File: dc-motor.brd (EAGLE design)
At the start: 160 x 100 mm, 0 parts

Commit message: Erste Version des Schaltplans (Noch nicht fertig)
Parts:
- added C1, C10, C13, C14, C3, C9: 100nF, Capacitor:0805
- added C11: 1µF, Capacitor:0805
- added C12: 0,22µF, Capacitor:0805
- added C2, C7, C8: 10nF, Capacitor:0805
- added C4: 100µF/50V, Capacitor:E5-13
- added C5: 47µF, Capacitor:E5-13
- added C6: 100µF, Capacitor:E5-13
- added D1: 1N4007, Diode:RM10DR1
- added D2: 1,5KB33CA, Diode:CB417-15
- added F1: F2A, fuse:F457
- added F2: T0,5A, fuse:F457
- added G1: 8MHz, Crystals:HC33U-V
- added H1, H2: MOUNT-PAD-ROUND3.0, Holes:3,0-PAD
- added IC1: MEGA8-P, atmel:DIL28-3
- added JP1, JP2, JP3: (no value), jumper:JP2Q
- added R1: (no value), DC-DC-converter:SIP3
- added R10, R3, R8, R9: 2k7, Resistor:0805
- added R11, R4, R6: 39k, Resistor:0805
- added R12, R5, R7: 10k, Resistor:0805
- added R13, R14, R15: 3,3k, Resistor:0805
- added R16, R17, R18, R19: 180R, Resistor:0805
- added R2: 0,05R, Resistor:SMS-0
- added R20, R21, R22, R23: 250R, Resistor:0805
- added S1: (no value), Switch:B3F-10XX
- added S2, S3: (no value), Switch:1_POL_ABGW
- added U$17: MAX4080, Sensorics:MAX4080
- added U$28: ACPL-247, Optoelectronic:SOIC16
- added U$3: DRV-8800, DRV-8800:TSSOP16
- added X1: (no value), con-subd:F09HP
- added X2: (no value), con-subd:M09HP
- added X3, X4: RIA_3POL, Connector:RIA_3POL
- added X5: RIA_2POL, Connector:RIA_2POL
- added X6: JUMP1-4, Connector:JUMP1-4
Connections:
- new net +24V: C5.+, D1.K, D2.C, F1.1, F2.2, R1.1, R11.2
- new net GND: C1.1, C10.1, C12.1, C14.1, C2.1, C4.-, C5.-, C6.-, C7.1, C8.1, C9.1, D1.A, D2.A, IC1.22, IC1.8, R1.2, R10.1, R12.1, R15.2, R3.1, R5.1, R7.1, R8.1, R9.1, S1.3, S1.4, U$17.4, U$28.2, U$28.4, U$28.6, U$28.8, U$3.12, U$3.2, X1.G1, X1.G2, X2.6, X2.7, X2.G2, X5.P$2, X6.4
- new net N$1: F1.2, X2.1, X5.P$1
- new net N$10: C13.1, C14.2, C4.+, R2.2, U$17.8, U$3.8
- new net N$11: IC1.18, R6.1, R7.2
- new net N$12: R6.2, X2.9
- new net N$13: R4.2, X2.8
- new net N$14: IC1.23, U$17.5
- new net N$15: IC1.17, R8.2, S3.S1
- new net N$16: C3.1
- new net N$17: IC1.16, R3.2, S2.S1
- new net N$18: IC1.15, JP1.1, JP1.3, R9.2
- new net N$19: JP1.2, JP2.2, X1.3
- new net N$2: G1.2, IC1.9
- new net N$20: JP1.4, JP2.4, X1.2
- new net N$21: H1.B3,0
- new net N$22: IC1.1, S1.1, S1.2
- new net N$23: C8.2, IC1.20
- new net N$24: C10.2, H2.B3,0
- new net N$25: IC1.14, JP2.1, JP2.3, R10.2
- new net N$26: C11.2, U$3.10
- new net N$27: C11.1, U$3.11
- new net N$28: C12.2, U$3.14
- new net N$29: C13.2, U$3.13
- new net N$3: G1.1, IC1.10
- new net N$30: IC1.25
- new net N$31: R23.1, U$3.4
- new net N$32: R21.1, U$3.1
- new net N$33: R14.1, U$3.15
- new net N$34: R13.1, R20.1, U$3.3
- new net N$35: U$28.15
- new net N$36: R15.1, U$3.7
- new net N$38: IC1.11, R16.1
- new net N$39: IC1.6, R19.1
- new net N$4: IC1.2, X6.1
- new net N$40: IC1.5, R18.2
- new net N$41: R17.2
- new net N$42: R16.2, U$28.1
- new net N$43: R17.1, U$28.3
- new net N$44: R18.1, U$28.5
- new net N$45: R19.2, U$28.7
- new net N$46: R23.2, U$28.13
- new net N$47: R21.2, U$28.11
- new net N$48: R22.1, U$3.16
- new net N$49: R20.2, U$28.9
- new net N$5: JP3.1, JP3.4, U$3.6, X1.4
- new net N$50: IC1.24, R11.1, R12.2
- new net N$51: IC1.26
- new net N$52: IC1.27
- new net N$53: IC1.28
- new net N$6: F2.1, R2.1, U$17.1
- new net N$7: JP3.2, JP3.3, U$3.9, X1.5
- new net N$8: IC1.3, X6.2
- new net N$9: IC1.19, R4.1, R5.2
- new net VDD: C1.2, C2.2, C3.2, C6.+, C7.2, IC1.21, IC1.7, R1.3, R13.2, R14.2, S2.S2, S3.S2, U$17.2, U$28.10, U$28.12, U$28.14, U$28.16, X1.1, X6.3

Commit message: Schaltplan Fertig
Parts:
- added C15, C16: 15pF, Capacitor:0805
- added H3: MOUNT-HOLE3.2, Holes:3,2
- added R24, R28, R31, R32: 2k2, Resistor:0805
- added R25, R26, R29, R30: 10R, Resistor:0805
- added R27: 180R, Resistor:0805
- added R33, R34, R35: 2k7, Resistor:0805
- added U$34: ACPL-247, Optoelectronic:SOIC16
- added U$35, U$38: IRF7341, Transistor:SO08-IRF
- added X7, X8: PFVERB10, Connector:PFVERB10
- C11: value 1µF -> 100nF
- IC1: value MEGA8-P -> MEGA32-A; device atmel:DIL28-3 -> atmel:TQFP44
- R13: value 3,3k -> 2k7
- moved JP3 224.9 mm to (130.8, 21.6)
- moved C13 220.3 mm to (111.8, 16.5)
- moved R2 215.6 mm to (114.3, 35.6)
- moved R13 214.5 mm to (104.1, 21.6)
- moved JP2 214.5 mm to (130.8, 43.2)
- moved X2 213.2 mm to (149.9, 49.5), turned to 90 degrees
- moved C12 201.7 mm to (116.8, 16.5), turned to 180 degrees
- moved R6 200.7 mm to (134.6, 54.6)
- moved R7 200.7 mm to (129.5, 54.6)
- moved X4 199.3 mm to (157.5, 94.0), turned to 90 degrees
- moved U$3 194.8 mm to (113.0, 22.9), turned to 180 degrees
- moved R4 191.6 mm to (134.6, 50.8)
- moved R5 191.6 mm to (129.5, 50.8)
- moved R21 189.4 mm to (123.2, 25.4), turned to 90 degrees
- moved X5 189.1 mm to (129.5, 8.89), turned to 270 degrees
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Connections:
- removed net N$14 (its old number): IC1.23, U$17.5
- removed net N$22: IC1.1, S1.1, S1.2
- removed net N$30: IC1.25
- removed net N$32 (its old number): R21.1, U$3.1
- removed net N$39: IC1.6, R19.1
- removed net N$40: IC1.5, R18.2
- removed net N$41: R17.2
- removed net N$51: IC1.26
- removed net N$52: IC1.27
- removed net N$53: IC1.28
- new net ENDLAGE_A: IC1.41, R32.1, U$35.2
- new net ENDLAGE_B: IC1.40, R31.1, U$35.4
- new net FAEHRTNACHA: IC1.36, X7.5
- new net FAEHRTNACHB: IC1.35, X7.6
- new net LOCAL/REMOTE: IC1.33, X7.8
- new net MISO: IC1.2, R18.2, X8.3
- new net MOSI: IC1.1, R19.1, X8.9
- new net MOTORSICHERUNGLED: IC1.37, X7.4
- new net MOTORSTOP: IC1.34, X7.7
- new net N$10: IC1.31, U$17.5
- new net N$37: U$34.14, X2.5
- new net N$54: R26.2, X2.4
- new net N$55: R25.2, X2.3
- new net N$57: U$34.3
- new net N$58: U$34.13, U$38.1, U$38.3
- new net N$59: R25.1, U$38.5, U$38.6
- new net N$60: C8.2, IC1.27
- new net N$61: R27.2, U$34.4
- new net N$62: R26.1, U$38.7, U$38.8
- new net N$67: R29.1, X3.P$1
- new net N$68: R30.1, X4.P$1
- new net N$69: R30.2, U$35.5, U$35.6
- new net N$70: U$35.3, X4.P$2
- new net N$71: R29.2, U$35.7, U$35.8
- new net N$72: U$35.1, X3.P$2
- new net N$77: R21.1, R35.2, U$3.1
- new net RESET: IC1.4, S1.1, S1.2, X8.6
- new net SCK: IC1.3, R17.2, X8.1
- net +24V: now also X7.3
- net GND: now also C15.2, C16.2, C3.1, IC1.18, IC1.28, IC1.39, IC1.6, R13.1, R24.2, R27.1, R28.2, R31.2, R32.2, R33.1, R34.1, R35.1, X3.P$3, X4.P$3, X7.10, X8.10, X8.2; no longer IC1.22, IC1.8
- net N$11: now also IC1.22; no longer IC1.18
- net N$15: now also IC1.23; no longer IC1.17
- net N$16: now also IC1.42, R24.1, U$38.2; no longer C3.1
- net N$17: now also IC1.24; no longer IC1.16
- net N$18: now also IC1.25; no longer IC1.15
- net N$19: now also X7.1
- net N$2: now also C15.1, G1.1, IC1.8; no longer G1.2, IC1.9
- net N$20: now also X7.2
- net N$21: now also C9.2
- net N$23: now also IC1.43, R28.1, U$38.4; no longer C8.2, IC1.20
- net N$25: now also IC1.26; no longer IC1.14
- net N$3: now also C16.1, G1.2, IC1.7; no longer G1.1, IC1.10
- net N$31: now also R34.2
- net N$34: now also R13.2; no longer R13.1
- net N$35: now also R22.2
- net N$38: now also IC1.44; no longer IC1.11
- net N$4: now also IC1.9; no longer IC1.2
- net N$48: now also R33.2
- net N$50: now also IC1.32; no longer IC1.24
- net N$6: now also IC1.30
- net N$8: now also IC1.10; no longer IC1.3
- net N$9: now also IC1.21; no longer IC1.19
- net VDD: now also IC1.17, IC1.29, IC1.38, IC1.5, X7.9, X8.4; no longer IC1.21, IC1.7, R13.2
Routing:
- net N$1: track 0.00 -> 192.5 mm, vias 0 -> 1
- net +24V: track 0.00 -> 84.8 mm
- net VDD: track 0.00 -> 41.4 mm
- net N$46: track 0.00 -> 9.42 mm
- net N$24: track 0.00 -> 9.21 mm
- net N$21: track 0.00 -> 9.21 mm
- net N$45: track 0.00 -> 8.14 mm
- net N$44: track 0.00 -> 7.51 mm
- net N$35: track 0.00 -> 7.18 mm
- net N$43: track 0.00 -> 5.74 mm
- net N$42: track 0.00 -> 5.29 mm
- net GND: track 0.00 -> 0.72 mm
- added copper zone on layer 1, net GND
- added copper zone on layer 16, net GND

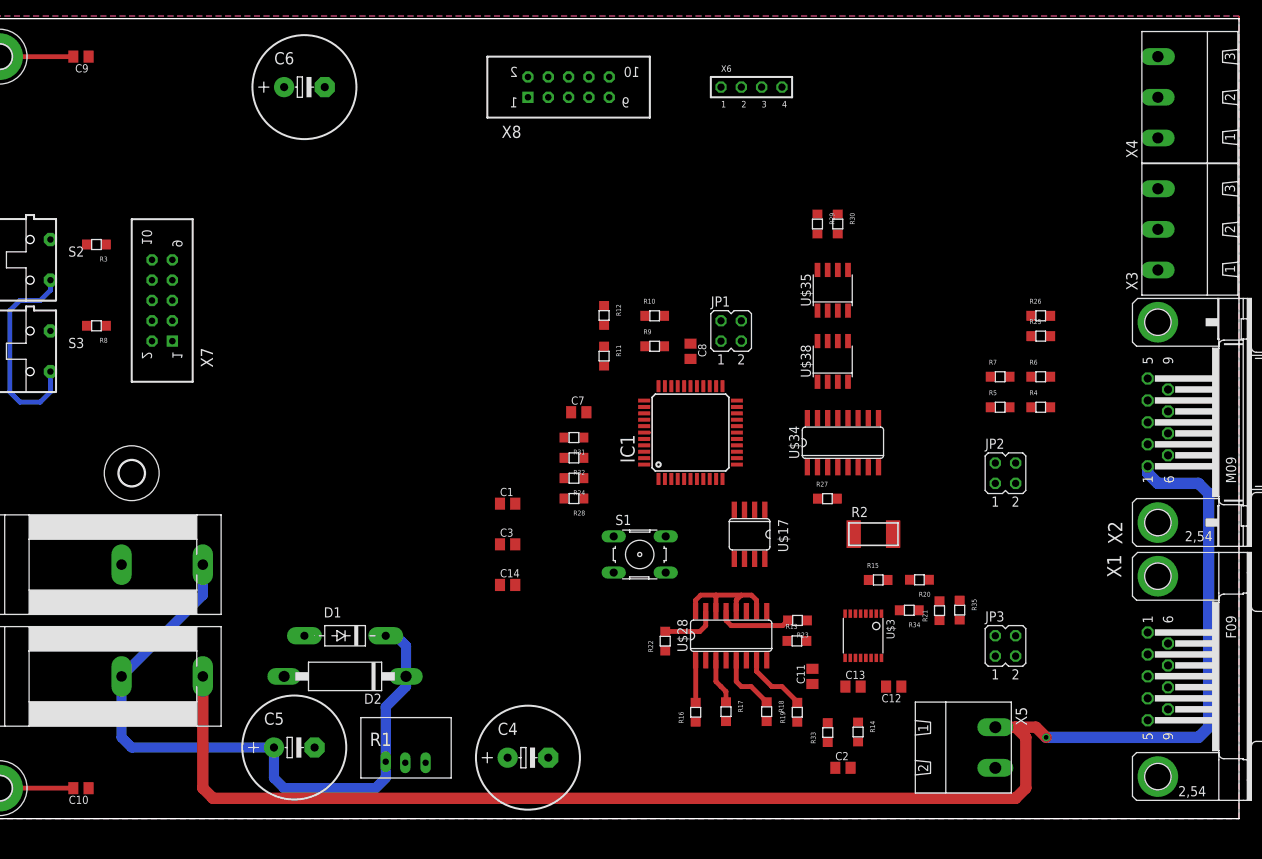
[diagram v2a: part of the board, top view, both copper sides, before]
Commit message: Schaltplan Verbessert und mit dem Layout begonnen
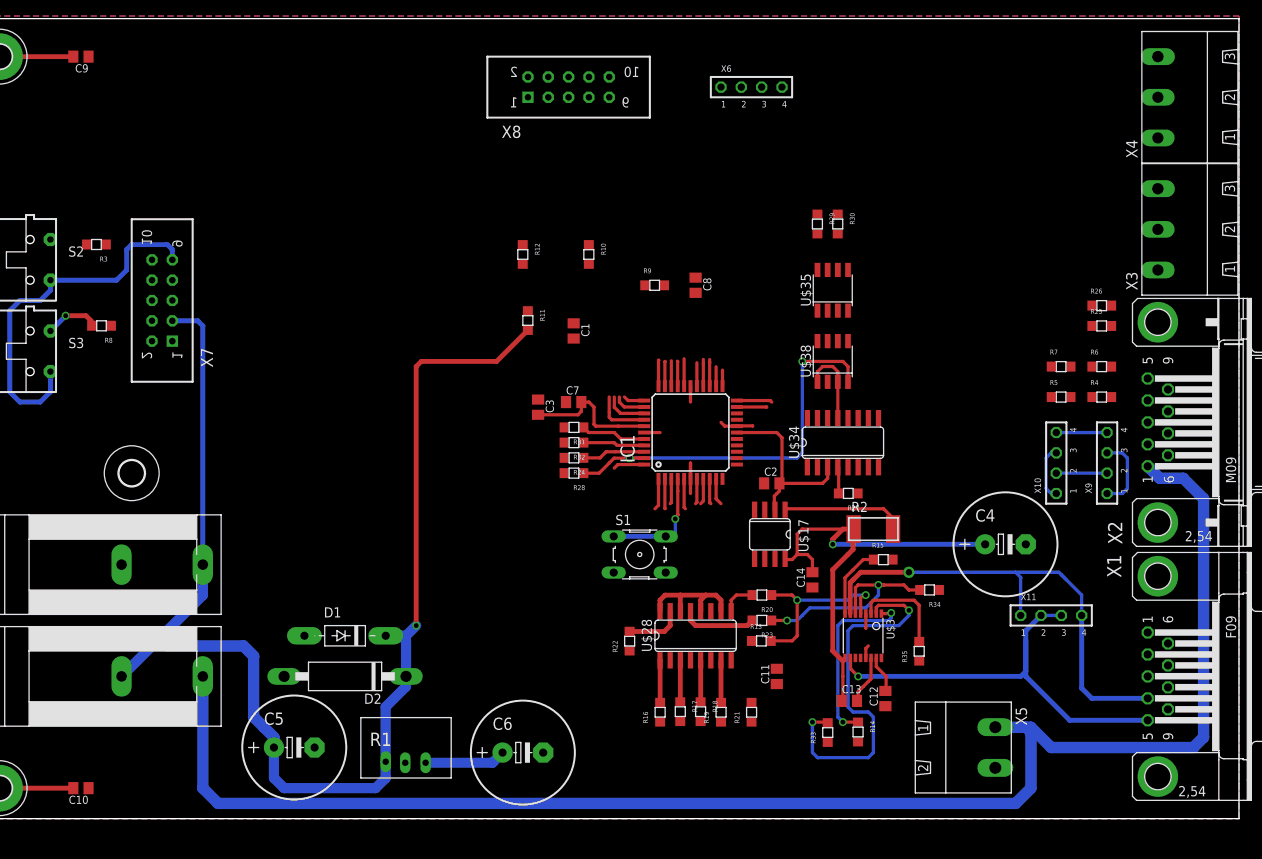
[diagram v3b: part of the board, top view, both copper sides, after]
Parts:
- removed JP1, JP2, JP3: (no value), jumper:JP2Q
- added X10, X11, X9: JUMP1-4, Connector:JUMP1-4
- moved C6 87.6 mm to (70.5, 8.26)
- moved C4 65.4 mm to (130.8, 34.3)
- moved C14 38.1 mm to (106.7, 29.8), turned to 90 degrees
- moved C2 36.7 mm to (101.6, 41.9)
- moved R21 26.7 mm to (99.7, 12.7)
- moved C1 23.1 mm to (76.8, 61.0), turned to 270 degrees
- moved R20 19.8 mm to (101.0, 28.6)
- moved C3 17.6 mm to (72.4, 51.4), turned to 270 degrees
- moved R12 12.7 mm to (69.8, 71.1)
- moved R10 12.1 mm to (78.1, 71.1), turned to 270 degrees
- moved R11 10.5 mm to (70.5, 62.9)
- moved R19 9.52 mm to (95.9, 12.7)
- moved C8 8.28 mm to (92.1, 66.7)
- moved R18 8.25 mm to (92.1, 14.0)
- moved R25 7.73 mm to (142.2, 61.0)
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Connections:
- removed net N$19 (its old number): JP1.2, JP2.2, X1.3, X7.1
- removed net N$57: U$34.3
- removed net N$7: JP3.2, JP3.3, U$3.9, X1.5
- new net N$22: X1.3, X10.2, X7.1, X9.2
- new net N$30: U$3.10, X1.5, X11.2, X11.3
- net GND: now also U$3.13, U$3.4; no longer U$3.12, U$3.2
- net N$18: now also X10.1, X10.3; no longer JP1.1, JP1.3
- net N$20: now also X10.4, X9.4; no longer JP1.4, JP2.4
- net N$25: now also X9.1, X9.3; no longer JP2.1, JP2.3
- net N$26: now also U$3.11; no longer U$3.10
- net N$27: now also U$3.12; no longer U$3.11
- net N$28: now also U$3.15; no longer U$3.14
- net N$29: now also U$3.14; no longer U$3.13
- net N$31: now also U$3.6; no longer U$3.4
- net N$32: now also U$3.9; no longer U$3.8
- net N$33: now also U$3.1; no longer U$3.15
- net N$34: now also U$3.5; no longer U$3.3
- net N$36: now also U$3.8; no longer U$3.7
- net N$48: now also U$3.2; no longer U$3.16
- net N$5: now also U$3.7, X11.1, X11.4; no longer JP3.1, JP3.4, U$3.6
- net N$77: now also U$3.3; no longer U$3.1
- net VDD: now also U$34.3
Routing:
- net +24V: track 84.8 -> 167.9 mm, vias 0 -> 1
- net VDD: track 41.4 -> 119.0 mm
- net N$32: track 0.00 -> 62.4 mm, vias 0 -> 1
- net N$5: track 0.00 -> 61.5 mm, vias 0 -> 1
- net N$30: track 0.00 -> 56.2 mm, vias 0 -> 1
- net N$23: track 0.00 -> 49.5 mm, vias 0 -> 3
- net N$48: track 0.00 -> 45.9 mm, vias 0 -> 2
- net N$31: track 0.00 -> 28.3 mm, vias 0 -> 2
- net N$33: track 0.00 -> 23.2 mm, vias 0 -> 2
- net N$34: track 0.00 -> 23.1 mm, vias 0 -> 2
- net N$6: track 0.00 -> 18.9 mm
- net GND: track 0.72 -> 17.5 mm
- net RESET: track 0.00 -> 14.9 mm, vias 0 -> 1
- net N$25: track 0.00 -> 12.8 mm
- net N$77: track 0.00 -> 12.3 mm
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
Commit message: Schaltplan erweitert
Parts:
- G1: device Crystals:HC33U-V -> Crystals:HC18U-V
- moved C16 200.2 mm to (87.0, 36.8), turned to 180 degrees
- moved G1 199.7 mm to (90.2, 32.4)
- moved C15 128.4 mm to (96.5, 36.8)
- moved R12 41.4 mm to (66.7, 29.8), turned to 180 degrees
- moved R11 34.2 mm to (61.6, 29.8), turned to 180 degrees
- moved C11 11.3 mm to (113.0, 14.6), turned to 180 degrees
- moved S1 8.89 mm to (76.2, 33.0)
- moved D1 5.24 mm to (54.6, 24.1)
- moved C12 3.47 mm to (118.3, 17.4), turned to 180 degrees
- moved C13 3.18 mm to (111.3, 11.5)
- moved R33 3.17 mm to (109.2, 6.99)
- moved R14 3.17 mm to (111.8, 8.26)
- moved D2 2.54 mm to (50.8, 17.8)
- moved R25 2.54 mm to (142.2, 63.5)
- moved R26 2.54 mm to (142.2, 61.0)
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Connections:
- net N$6: no longer IC1.30
- net VDD: now also IC1.30
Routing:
- net VDD: track 119.0 -> 319.4 mm, vias 0 -> 1
- net N$67: track 0.00 -> 79.8 mm
- net N$70: track 0.00 -> 75.4 mm
- net N$50: track 3.10 -> 58.2 mm
- net N$77: track 12.3 -> 65.3 mm
- net N$72: track 0.00 -> 50.3 mm
- net N$68: track 0.00 -> 49.2 mm
- net N$37: track 0.00 -> 47.2 mm
- net +24V: track 167.9 -> 124.7 mm, vias 1 -> 0
- net N$62: track 0.00 -> 39.3 mm
- net N$20: track 6.35 -> 44.9 mm
- net N$48: track 45.9 -> 83.3 mm, vias 2 -> 3
- net N$59: track 0.00 -> 35.5 mm
- net N$22: track 6.35 -> 37.8 mm
- net N$55: track 0.00 -> 28.3 mm
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
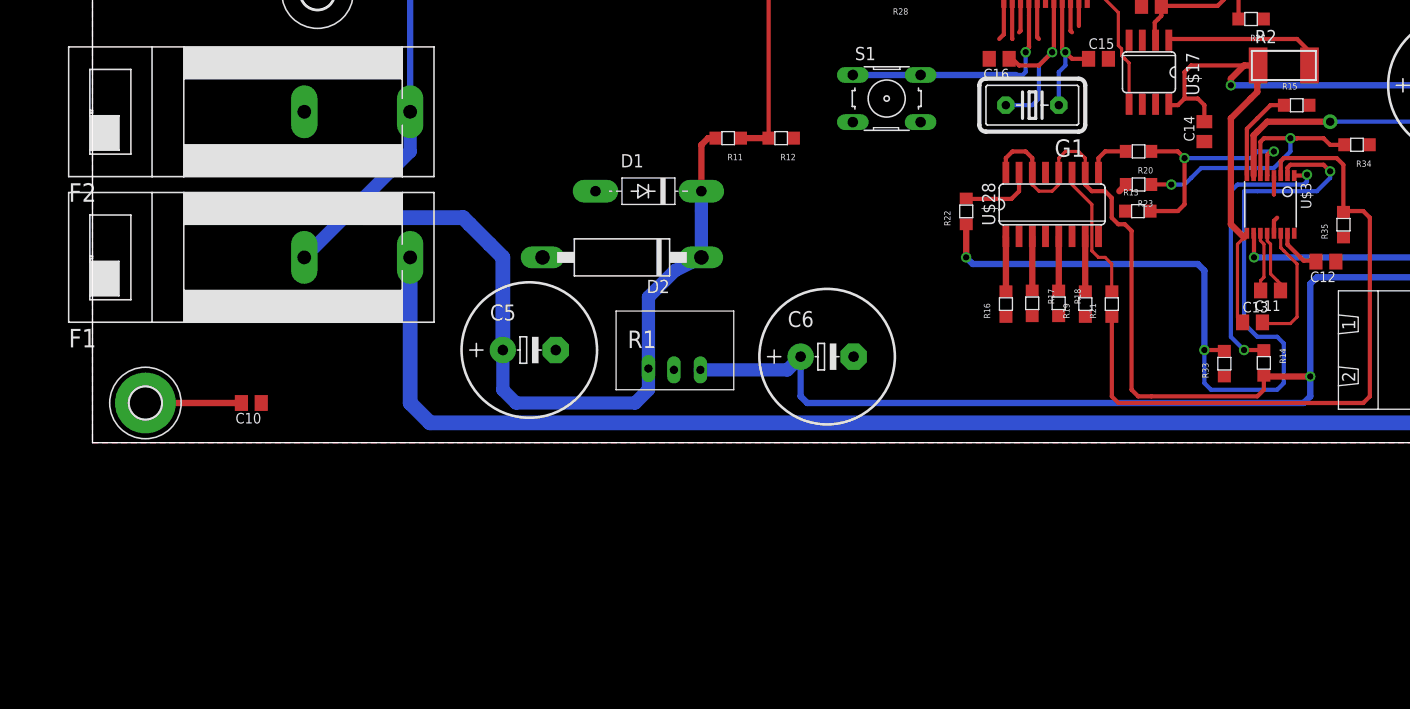
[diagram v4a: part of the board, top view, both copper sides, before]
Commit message: ADC wiring changed.
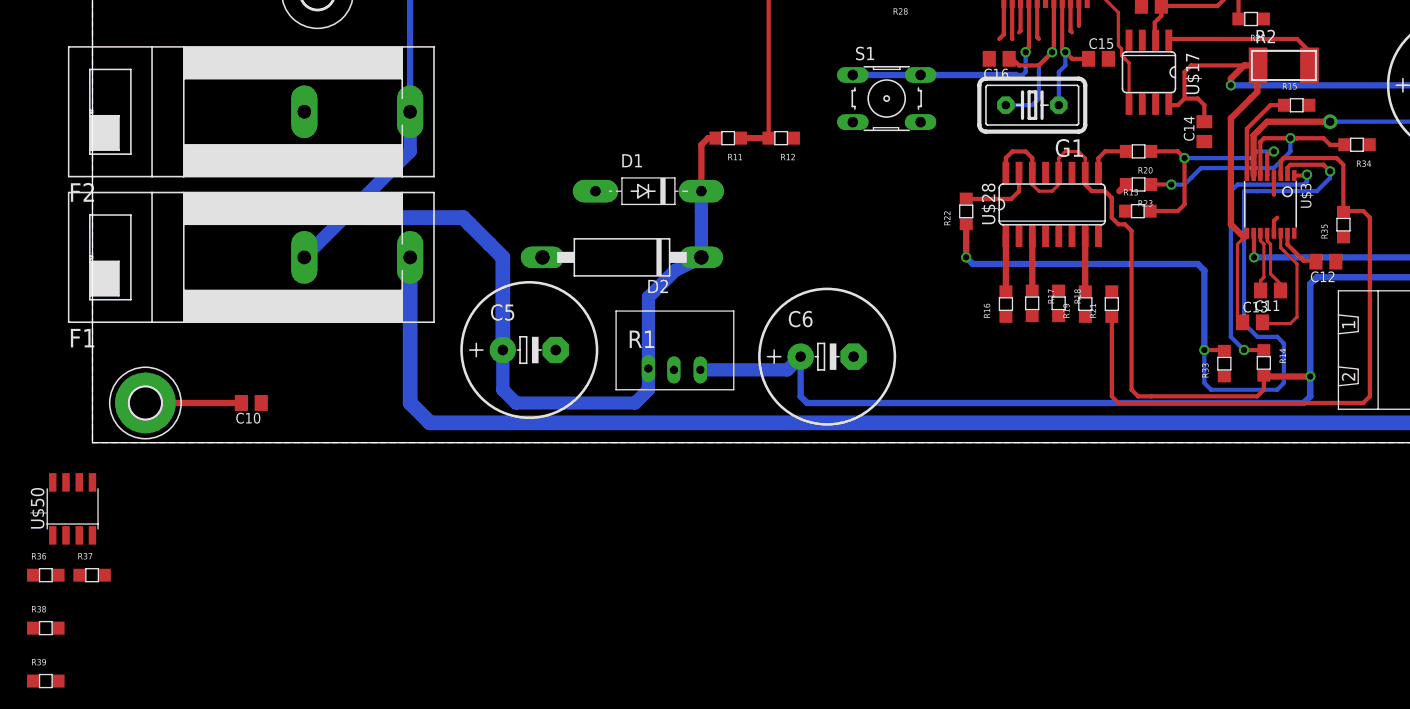
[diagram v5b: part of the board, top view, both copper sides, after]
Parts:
- added R36: 10R, Resistor:0805
- added R37: 100k, Resistor:0805
- added R38: 39k, Resistor:0805
- added R39: 10k, Resistor:0805
- added U$50: IRF7341, Transistor:SO08-IRF
- R16, R17, R18, R19, R27: value 180R -> 330R
- R24, R28, R31, R32: value 2k2 -> 100k
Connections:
- new net N$39: R36.2
- new net PC_LOCAL/REMOTE: R36.1, X2.2
- new net VOLTAGE_FUSE: IC1.30, R38.1, R39.2
- net +24V: now also U$50.1
- net GND: now also R37.2, R39.1
- net LOCAL/REMOTE: now also R37.1, U$50.2
- net N$6: now also R38.2
- net VDD: no longer IC1.30
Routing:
- net N$47: track 13.4 -> 0.00 mm
- net N$7: track 5.22 -> 0.00 mm
